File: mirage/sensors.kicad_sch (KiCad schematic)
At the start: 2 parts, among them U2 MS560702BA03-50, U3 ADXL375BCCZ-RL7

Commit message: feat: initialize structure
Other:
- moved on the sheet: U2, U3
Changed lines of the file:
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@@
 	(symbol
 		(lib_id "EasyEDA:MS560702BA03-50")
-		(at 67.31 38.1 0)
+		(at 69.85 40.64 0)
 		(unit 1)
 		(exclude_from_sim no)
@@
 		(fields_autoplaced yes)
 		(property "Reference" "U2"
-			(at 67.31 26.67 0)
+			(at 69.85 29.21 0)
 			(effects
 				(font
@@
 		)
 		(property "Value" "MS560702BA03-50"
-			(at 67.31 29.21 0)
+			(at 69.85 31.75 0)
 			(effects
 				(font
@@
 		)
 		(property "Footprint" "EasyEDA:SENSOR-SMD_MS560702BA03-50"
-			(at 67.31 49.53 0)
+			(at 69.85 52.07 0)
 			(effects
 				(font
@@
 		)
 		(property "Datasheet" "https://lcsc.com/product-detail/Pre-ordered-Products_TE-Connectivity_MS560702BA03-50_TE-Connectivity-MS560702BA03-50_C97627.html"
-			(at 67.31 52.07 0)
+			(at 69.85 54.61 0)
 			(effects
 				(font
@@
 		)
 		(property "Description" ""
-			(at 67.31 38.1 0)
+			(at 69.85 40.64 0)
 			(effects
 				(font
@@
 		)
 		(property "LCSC Part" "C97627"
-			(at 67.31 54.61 0)
+			(at 69.85 57.15 0)
 			(effects
 				(font
@@
 	(symbol
 		(lib_id "EasyEDA:ADXL375BCCZ-RL7")
-		(at 78.74 78.74 0)
+		(at 68.58 81.28 0)
 		(unit 1)
 		(exclude_from_sim no)
@@
 		(fields_autoplaced yes)
 		(property "Reference" "U3"
-			(at 78.74 63.5 0)
+			(at 68.58 66.04 0)
 			(effects
 				(font
@@
 		)
 		(property "Value" "ADXL375BCCZ-RL7"
-			(at 78.74 66.04 0)
+			(at 68.58 68.58 0)
 			(effects
 				(font
@@
 		)
 		(property "Footprint" "EasyEDA:LGA-14_L5.0-W3.0-P0.80-BL"
-			(at 78.74 93.98 0)
+			(at 68.58 96.52 0)
 			(effects
 				(font
@@
 		)
 		(property "Datasheet" "https://lcsc.com/product-detail/New-Arrivals_Analog-Devices-ADI-ADXL375BCCZ-RL7_C481898.html"
-			(at 78.74 96.52 0)
+			(at 68.58 99.06 0)
 			(effects
 				(font
@@
 		)
 		(property "Description" ""
-			(at 78.74 78.74 0)
+			(at 68.58 81.28 0)
 			(effects
 				(font
@@
 		)
 		(property "LCSC Part" "C481898"
-			(at 78.74 99.06 0)
+			(at 68.58 101.6 0)
 			(effects
 				(font

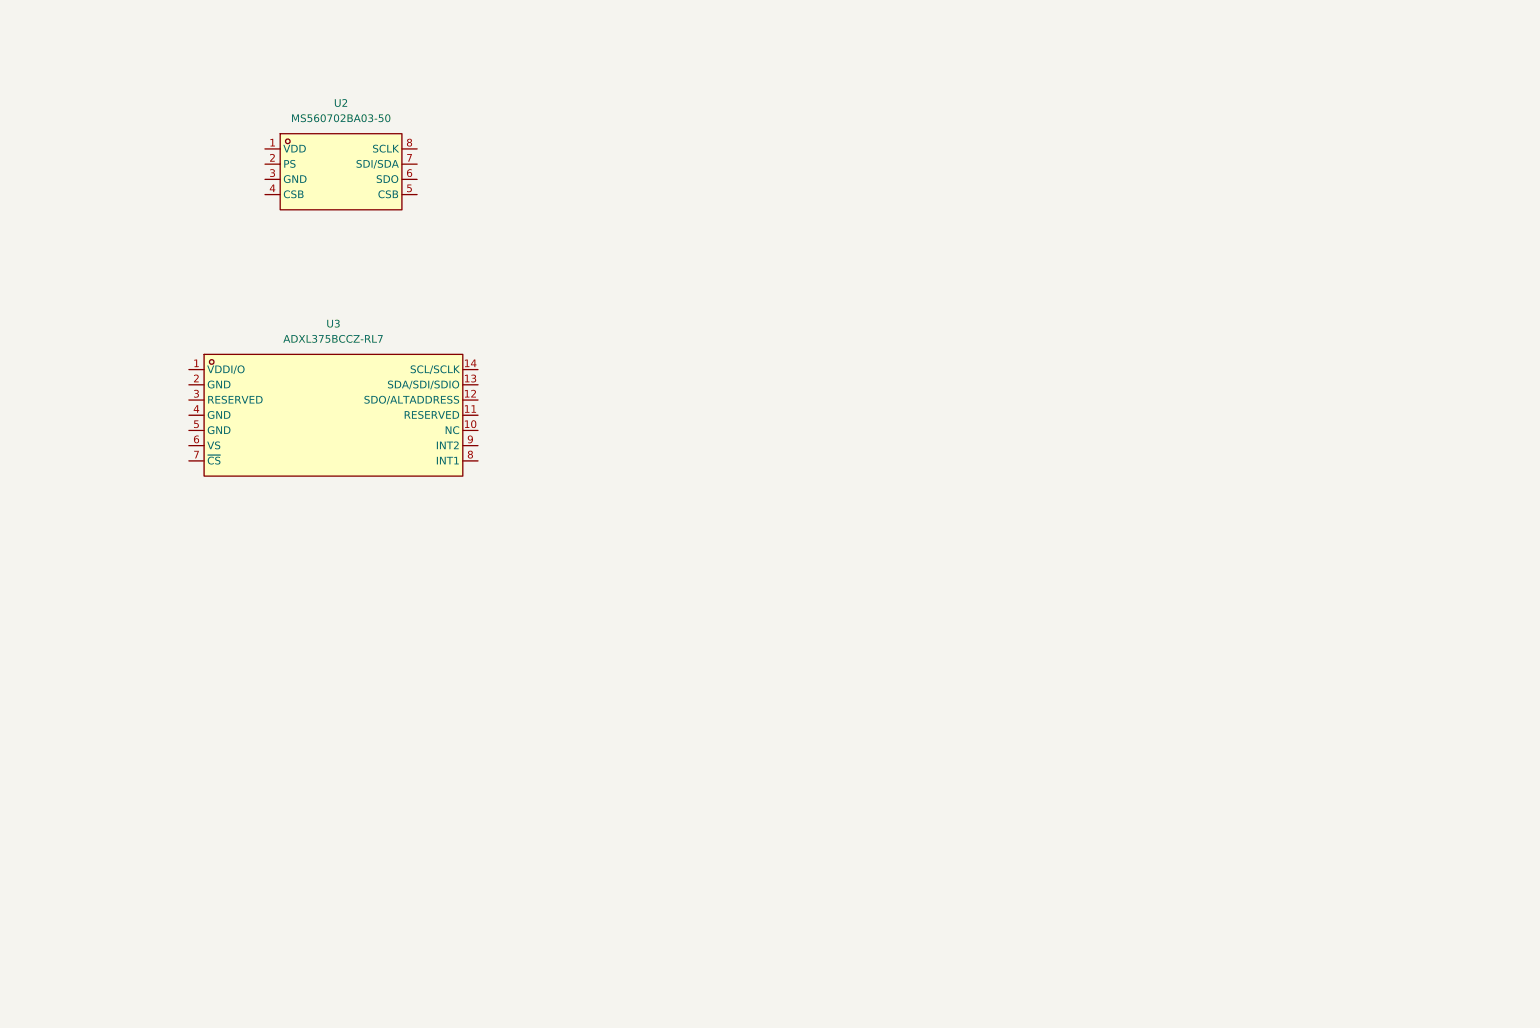
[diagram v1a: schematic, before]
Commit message: feat(sensor): fundamental sensor lists
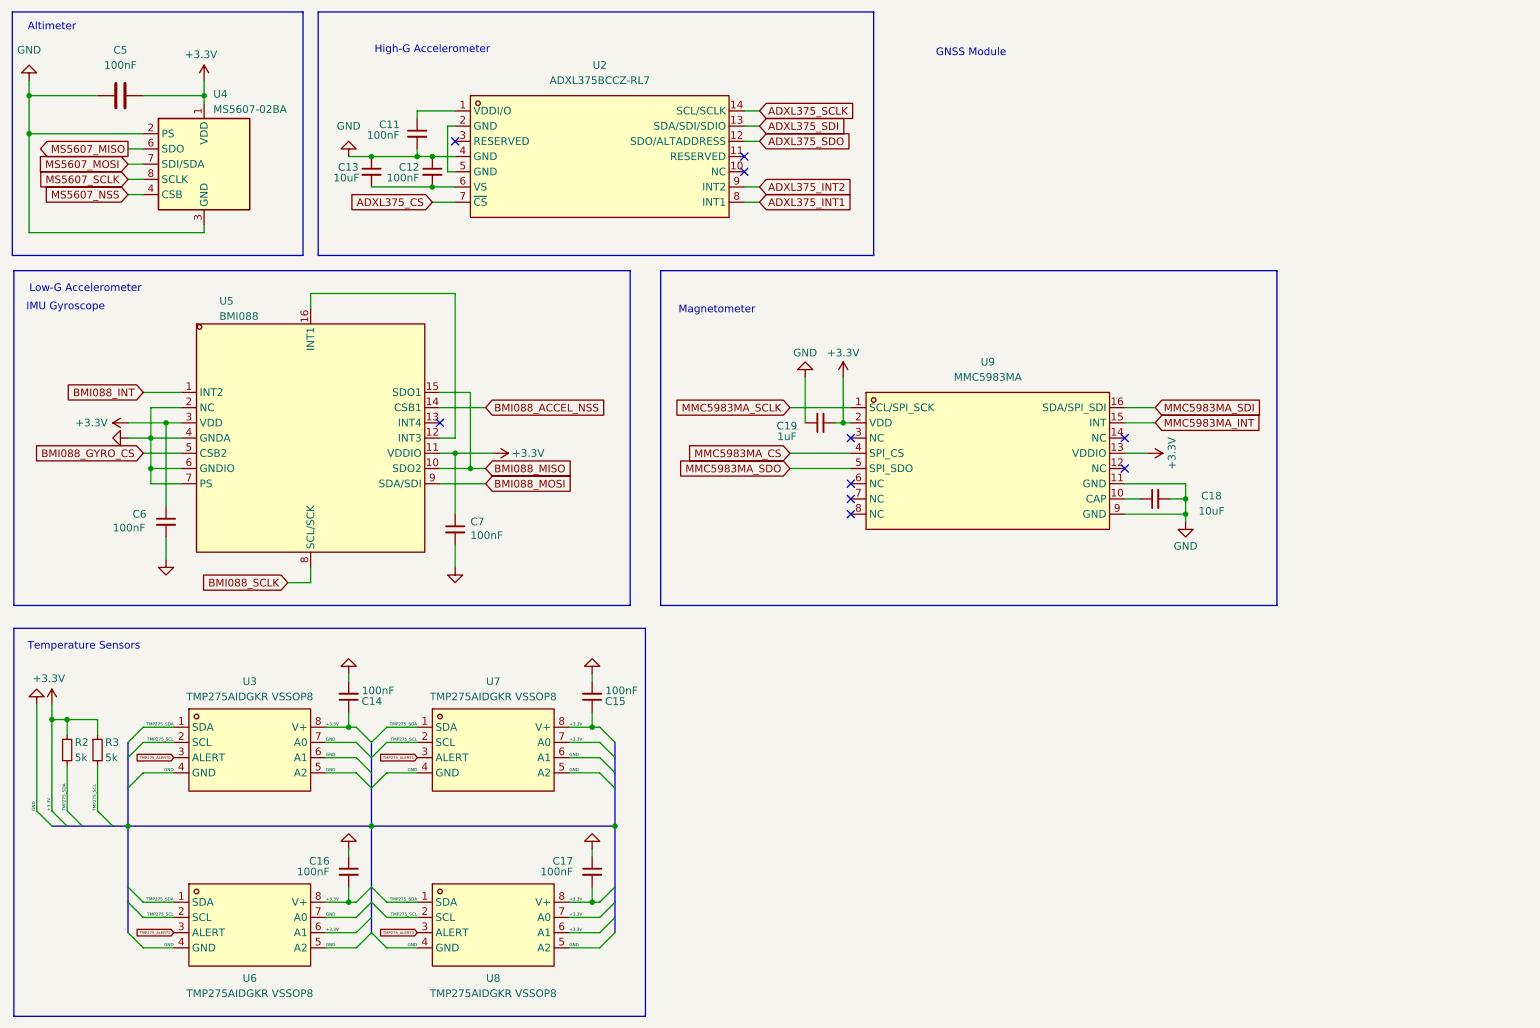
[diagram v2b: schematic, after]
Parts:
- removed U2: MS560702BA03-50, EasyEDA:SENSOR-SMD_MS560702BA03-50, symbol EasyEDA:MS560702BA03-50
- removed U3: ADXL375BCCZ-RL7, EasyEDA:LGA-14_L5.0-W3.0-P0.80-BL, symbol EasyEDA:ADXL375BCCZ-RL7
- added C11, C12, C14, C15, C17, C6, C7: 100nF, Capacitor_SMD:C_0402_1005Metric, symbol Device:C_Small
- added C13: 10uF, Capacitor_SMD:C_0402_1005Metric, symbol Device:C_Small
- added C16: 100nF, Capacitor_SMD:C_0504_1310Metric_Pad0.83x1.28mm_HandSolder, symbol Device:C_Small
- added C18: 10uF, symbol Device:C_Small
- added C19: 1uF, symbol Device:C_Small
- added C5: 100nF, Capacitor_SMD:C_0402_1005Metric, symbol Device:C
- added R2, R3: 5k, Resistor_SMD:R_0402_1005Metric, symbol Device:R_Small
- added U2: ADXL375BCCZ-RL7, EasyEDA:LGA-14_L5.0-W3.0-P0.80-BL, symbol EasyEDA:ADXL375BCCZ-RL7
- added U3, U6, U7, U8: TMP275AIDGKR VSSOP8, EasyEDA:VSSOP-8_L3.0-W3.0-P0.65-LS5.0-BL, symbol EasyEDA:TMP275AIDGKRVSSOP8
- added U4: MS5607-02BA, Package_LGA:LGA-8_3x5mm_P1.25mm, symbol Sensor_Pressure:MS5607-02BA
- added U5: BMI088, EasyEDA:LGA-16_L4.5-W3.0-P0.50-BL, symbol EasyEDA:BMI088
- added U9: MMC5983MA, EasyEDA:LGA-16_L3.0-W3.0-P0.50-BL_SQ, symbol EasyEDA:MMC5983MA
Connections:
- new net: C18.1, U9.10 (CAP)
- new net: U5.12 (INT3), U5.16 (INT1)
- new net: C12.2, C13.2, U2.6 (VS)
- new net: C11.1, U2.1 (VDDI/O)
- new net: U2.2 (GND), U2.5 (GND)
- new net +3.3V: C14.1, C15.1, C16.2, C17.2, C19.2, C5.2, C6.1, C7.1, R2.1, R3.1, U3.8 (V+), U4.1 (VDD), U5.11 (VDDIO), U5.3 (VDD), U6.6 (A1), U6.8 (V+), U7.7 (A0), U7.8 (V+), U8.6 (A1), U8.7 (A0), U8.8 (V+), U9.13 (VDDIO), U9.2 (VDD)
- new net ADXL375_CS: U2.7 (~{CS})
- new net ADXL375_INT1: U2.8 (INT1)
- new net ADXL375_INT2: U2.9 (INT2)
- new net ADXL375_SCLK: U2.14 (SCL/SCLK)
- new net ADXL375_SDI: U2.13 (SDA/SDI/SDIO)
- new net ADXL375_SDO: U2.12 (SDO/ALTADDRESS)
- new net BMI088_ACCEL_NSS: U5.14 (CSB1)
- new net BMI088_GYRO_CS: U5.5 (CSB2)
- new net BMI088_INT: U5.1 (INT2)
- new net BMI088_MISO: U5.10 (SDO2), U5.15 (SDO1)
- new net BMI088_MOSI: U5.9 (SDA/SDI)
- new net BMI088_SCLK: U5.8 (SCL/SCK)
- new net GND: C11.2, C12.1, C13.1, C14.2, C15.2, C16.1, C17.1, C18.2, C19.1, C5.1, C6.2, C7.2, U2.4 (GND), U3.4 (GND), U3.5 (A2), U3.6 (A1), U3.7 (A0), U4.2 (PS), U4.3 (GND), U5.2 (NC), U5.4 (GNDA), U5.6 (GNDIO), U5.7 (PS), U6.4 (GND), U6.5 (A2), U6.7 (A0), U7.4 (GND), U7.5 (A2), U7.6 (A1), U8.4 (GND), U8.5 (A2), U9.11 (GND), U9.9 (GND)
- new net MMC5983MA_CS: U9.4 (SPI_CS)
- new net MMC5983MA_INT: U9.15 (INT)
- new net MMC5983MA_SCLK: U9.1 (SCL/SPI_SCK)
- new net MMC5983MA_SDI: U9.16 (SDA/SPI_SDI)
- new net MMC5983MA_SDO: U9.5 (SPI_SDO)
- new net MS5607_MISO: U4.6 (SDO)
- new net MS5607_MOSI: U4.7 (SDI/SDA)
- new net MS5607_NSS: U4.4 (CSB), U4.5 (CSB)
- new net MS5607_SCLK: U4.8 (SCLK)
- new net TMP275_ALERT0: U3.3 (ALERT)
- new net TMP275_ALERT1: U7.3 (ALERT)
- new net TMP275_ALERT2: U6.3 (ALERT)
- new net TMP275_ALERT3: U8.3 (ALERT)
- new net TMP275_SCL: R3.2, U3.2 (SCL), U6.2 (SCL), U7.2 (SCL), U8.2 (SCL)
- new net TMP275_SDA: R2.2, U3.1 (SDA), U6.1 (SDA), U7.1 (SDA), U8.1 (SDA)
- no-connect marks 0 -> 10
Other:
- note added: "Altimeter"
- note added: "GNSS Module"
- note added: "High-G Accelerometer"
- note added: "IMU Gyroscope"
- note added: "Low-G Accelerometer"
- note added: "Magnetometer"
- note added: "Temperature Sensors"
- title: (none) -> Sensors

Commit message: feat: connectors
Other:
- note removed: "GNSS Module"
- moved on the sheet: C11, C12, C13, C14, C15, C16, C17, C18, C19, C5, C6, C7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
